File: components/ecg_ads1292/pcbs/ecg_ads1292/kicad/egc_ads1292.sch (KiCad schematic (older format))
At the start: 27 parts, among them J1 n.p., J2 n.p., J3 n.p., J4 n.p., J5 Conn_02x10_Odd_Even, J6 Conn_02x10_Odd_Even

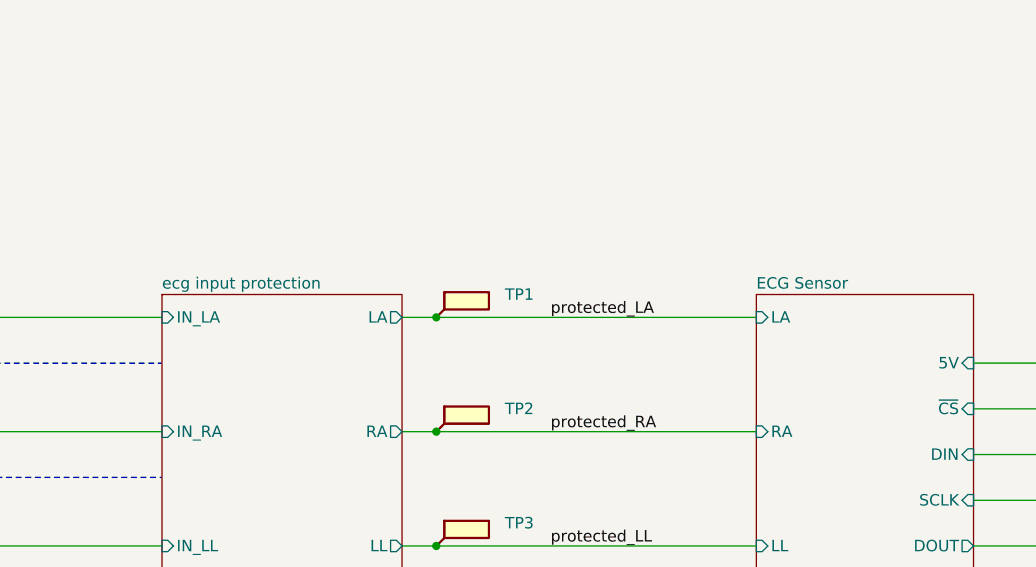
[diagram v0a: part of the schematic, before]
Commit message: first sim test with ne2 lib, blanks in sheet name removed
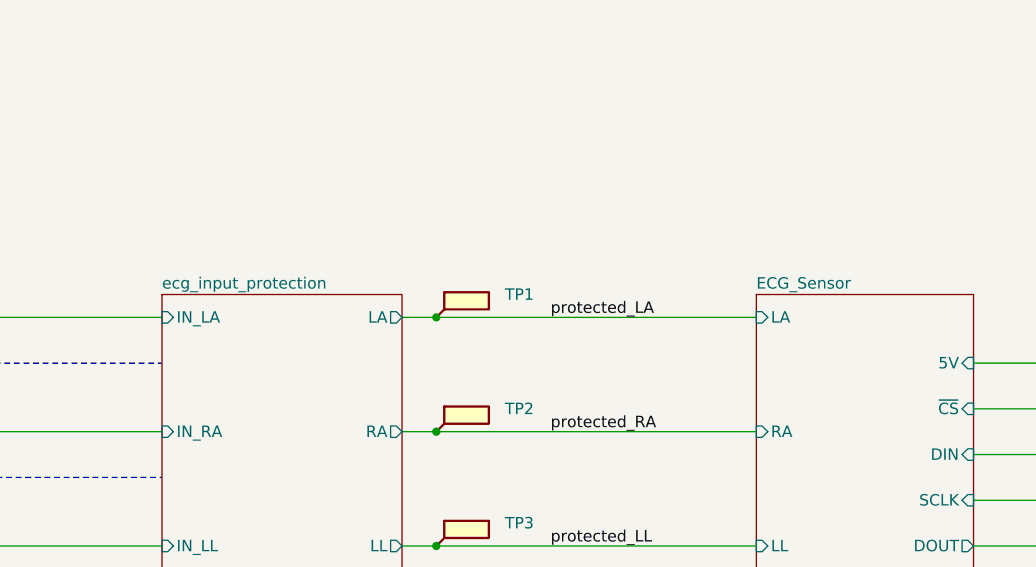
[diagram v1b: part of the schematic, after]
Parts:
- H1, H2, H3, H4, H5, J1, J2, J3, J4, J5, J6, R1, R2, R25, R26, R27, R29, R30, TP1, TP12, TP13, TP14, TP15, TP2, TP3, TP4, TP5: Spice_Netlist_Enabled (none) -> N
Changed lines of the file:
@@
 S 3600 2700 1050 1700
 U 5E80F57C
-F0 "ecg input protection" 50
+F0 "ecg_input_protection" 50
 F1 "ecg_input_protection.sch" 50
 F2 "LA" O R 4650 2800 50
@@
 F 2 "Connector_PinHeader_2.54mm:PinHeader_1x01_P2.54mm_Vertical" H 1700 2800 50  0001 C CNN
 F 3 "~" H 1700 2800 50  0001 C CNN
+F 4 "N" H 1700 2800 50  0001 C CNN "Spice_Netlist_Enabled"
 	1    1700 2800
 	-1   0    0    1
@@
 F 2 "Connector_PinHeader_2.54mm:PinHeader_1x01_P2.54mm_Vertical" H 1700 3300 50  0001 C CNN
 F 3 "~" H 1700 3300 50  0001 C CNN
+F 4 "N" H 1700 3300 50  0001 C CNN "Spice_Netlist_Enabled"
 	1    1700 3300
 	-1   0    0    1
@@
 F 2 "Connector_PinHeader_2.54mm:PinHeader_1x01_P2.54mm_Vertical" H 1700 3800 50  0001 C CNN
 F 3 "~" H 1700 3800 50  0001 C CNN
+F 4 "N" H 1700 3800 50  0001 C CNN "Spice_Netlist_Enabled"
 	1    1700 3800
 	-1   0    0    1
@@
 F 2 "Connector_PinHeader_2.54mm:PinHeader_1x01_P2.54mm_Vertical" H 1700 4300 50  0001 C CNN
 F 3 "~" H 1700 4300 50  0001 C CNN
+F 4 "N" H 1700 4300 50  0001 C CNN "Spice_Netlist_Enabled"
 	1    1700 4300
 	-1   0    0    1
@@
 F 5 "Farnell" H 2900 3300 50  0001 C CNN "Distributor"
 F 6 "1738916" H 2900 3300 50  0001 C CNN "Farnell"
+F 7 "N" H 8700 5150 50  0001 C CNN "Spice_Netlist_Enabled"
 	1    8700 5150
 	-1   0    0    1
@@
 S 6200 2700 950  2450
 U 5E8EE786
-F0 "ECG Sensor" 50
+F0 "ECG_Sensor" 50
 F1 "ecg_ads1292_sensor.sch" 50
 F2 "LA" I L 6200 2800 50
@@
 F 5 "Farnell" H 2900 2400 50  0001 C CNN "Distributor"
 F 6 "1738916" H 2900 2400 50  0001 C CNN "Farnell"
+F 7 "N" H 8700 4250 50  0001 C CNN "Spice_Netlist_Enabled"
 	1    8700 4250
 	-1   0    0    1
@@
 F 2 "TestPoint:TestPoint_Loop_D2.50mm_Drill1.0mm" H 5000 2800 50  0001 C CNN
 F 3 "~" H 5000 2800 50  0001 C CNN
+F 4 "N" H 4800 2800 50  0001 C CNN "Spice_Netlist_Enabled"
 	1    4800 2800
 	1    0    0    -1
@@
 F 2 "TestPoint:TestPoint_Loop_D2.50mm_Drill1.0mm" H 5000 3300 50  0001 C CNN
 F 3 "~" H 5000 3300 50  0001 C CNN
+F 4 "N" H 4800 3300 50  0001 C CNN "Spice_Netlist_Enabled"
 	1    4800 3300
 	1    0    0    -1
@@
 F 2 "TestPoint:TestPoint_Loop_D2.50mm_Drill1.0mm" H 5000 3800 50  0001 C CNN
 F 3 "~" H 5000 3800 50  0001 C CNN
+F 4 "N" H 4800 3800 50  0001 C CNN "Spice_Netlist_Enabled"
 	1    4800 3800
 	1    0    0    -1
@@
 F 2 "TestPoint:TestPoint_Loop_D2.50mm_Drill1.0mm" H 5000 4300 50  0001 C CNN
 F 3 "~" H 5000 4300 50  0001 C CNN
+F 4 "N" H 4800 4300 50  0001 C CNN "Spice_Netlist_Enabled"
 	1    4800 4300
 	1    0    0    -1
@@
 F 2 "TestPoint:TestPoint_Loop_D2.50mm_Drill1.0mm" H 7550 4550 50  0001 C CNN
 F 3 "~" H 7550 4550 50  0001 C CNN
+F 4 "N" H 7350 4550 50  0001 C CNN "Spice_Netlist_Enabled"
 	1    7350 4550
 	1    0    0    -1
@@
 F 2 "TestPoint:TestPoint_Loop_D2.50mm_Drill1.0mm" H 7550 4750 50  0001 C CNN
 F 3 "~" H 7550 4750 50  0001 C CNN
+F 4 "N" H 7350 4750 50  0001 C CNN "Spice_Netlist_Enabled"
 	1    7350 4750
 	1    0    0    -1
@@
 F 2 "TestPoint:TestPoint_Loop_D2.50mm_Drill1.0mm" H 7550 4950 50  0001 C CNN
 F 3 "~" H 7550 4950 50  0001 C CNN
+F 4 "N" H 7350 4950 50  0001 C CNN "Spice_Netlist_Enabled"
 	1    7350 4950
 	1    0    0    -1
@@
 F 2 "TestPoint:TestPoint_Loop_D2.50mm_Drill1.0mm" H 5000 4700 50  0001 C CNN
 F 3 "~" H 5000 4700 50  0001 C CNN
+F 4 "N" H 4800 4700 50  0001 C CNN "Spice_Netlist_Enabled"
 	1    4800 4700
 	1    0    0    -1
@@
 F 2 "TestPoint:TestPoint_Loop_D2.50mm_Drill1.0mm" H 7550 5450 50  0001 C CNN
 F 3 "~" H 7550 5450 50  0001 C CNN
+F 4 "N" H 7350 5450 50  0001 C CNN "Spice_Netlist_Enabled"
 	1    7350 5450
 	1    0    0    -1
@@
 F 2 "MountingHole:MountingHole_3.2mm_M3_ISO14580" H 800 6100 50  0001 C CNN
 F 3 "~" H 800 6100 50  0001 C CNN
+F 4 "N" H 800 6100 50  0001 C CNN "Spice_Netlist_Enabled"
 	1    800  6100
 	1    0    0    -1
@@
 F 2 "MountingHole:MountingHole_3.2mm_M3_ISO14580" H 800 6400 50  0001 C CNN
 F 3 "~" H 800 6400 50  0001 C CNN
+F 4 "N" H 800 6400 50  0001 C CNN "Spice_Netlist_Enabled"
 	1    800  6400
 	1    0    0    -1
@@
 F 2 "MountingHole:MountingHole_3.2mm_M3_ISO14580" H 800 6700 50  0001 C CNN
 F 3 "~" H 800 6700 50  0001 C CNN
+F 4 "N" H 800 6700 50  0001 C CNN "Spice_Netlist_Enabled"
 	1    800  6700
 	1    0    0    -1
@@
 F 2 "MountingHole:MountingHole_3.2mm_M3_ISO14580" H 800 6950 50  0001 C CNN
 F 3 "~" H 800 6950 50  0001 C CNN
+F 4 "N" H 800 6950 50  0001 C CNN "Spice_Netlist_Enabled"
 	1    800  6950
 	1    0    0    -1
@@
 F 2 "Resistor_SMD:R_0815_2038Metric_Pad1.53x4.00mm_HandSolder" V 2380 7050 50  0001 C CNN
 F 3 "" H 2450 7050 50  0001 C CNN
+F 4 "N" H 2450 7050 50  0001 C CNN "Spice_Netlist_Enabled"
 	1    2450 7050
 	0    1    1    0
@@
 F 2 "Resistor_SMD:R_0815_2038Metric_Pad1.53x4.00mm_HandSolder" V 2380 6650 50  0001 C CNN
 F 3 "" H 2450 6650 50  0001 C CNN
+F 4 "N" H 2450 6650 50  0001 C CNN "Spice_Netlist_Enabled"
 	1    2450 6650
 	0    1    1    0
@@
 F 2 "Resistor_SMD:R_0815_2038Metric_Pad1.53x4.00mm_HandSolder" V 2380 6250 50  0001 C CNN
 F 3 "" H 2450 6250 50  0001 C CNN
+F 4 "N" H 2450 6250 50  0001 C CNN "Spice_Netlist_Enabled"
 	1    2450 6250
 	0    1    1    0
@@
 F 2 "Resistor_SMD:R_0815_2038Metric_Pad1.53x4.00mm_HandSolder" V 2380 5850 50  0001 C CNN
 F 3 "" H 2450 5850 50  0001 C CNN
+F 4 "N" H 2450 5850 50  0001 C CNN "Spice_Netlist_Enabled"
 	1    2450 5850
 	0    1    1    0
@@
 F 2 "Resistor_SMD:R_0815_2038Metric_Pad1.53x4.00mm_HandSolder" V 2380 5450 50  0001 C CNN
 F 3 "" H 2450 5450 50  0001 C CNN
+F 4 "N" H 2450 5450 50  0001 C CNN "Spice_Netlist_Enabled"
 	1    2450 5450
 	0    1    1    0
@@
 F 2 "MountingHole:MountingHole_3.2mm_M3_Pad" H 1700 6750 50  0001 C CNN
 F 3 "~" H 1700 6750 50  0001 C CNN
+F 4 "N" H 1700 6750 50  0001 C CNN "Spice_Netlist_Enabled"
 	1    1700 6750
 	1    0    0    -1
@@
 F 2 "Connector_IDC:IDC-Header_2x10_P2.54mm_Vertical_Lock" H 10200 3500 50  0001 C CNN
 F 3 "~" H 10200 3500 50  0001 C CNN
+F 4 "N" H 10200 3500 50  0001 C CNN "Spice_Netlist_Enabled"
 	1    10200 3500
 	1    0    0    1
@@
 F 2 "Connector_IDC:IDC-Header_2x10_P2.54mm_Vertical_Lock" H 10150 1800 50  0001 C CNN
 F 3 "~" H 10150 1800 50  0001 C CNN
+F 4 "N" H 10150 1800 50  0001 C CNN "Spice_Netlist_Enabled"
 	1    10150 1800
 	1    0    0    1
